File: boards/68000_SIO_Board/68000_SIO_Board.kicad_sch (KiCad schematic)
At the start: 32 parts, among them J1 Conn_01x08, J10 Conn_02x08_Odd_Even, J11 Conn_01x08, J12 Conn_02x04_Odd_Even, J13 Conn_01x10, J14 Conn_02x02_Odd_Even, J2 Conn_01x06, J3 Conn_01x03, J4 Conn_02x10_Odd_Even, J5 Conn_01x06, J6 Conn_01x03, J7 Conn_01x06, J8 Conn_01x06, J9 Conn_01x08, M1 RC2014_40_PIN, U1 74LS138, U2 68681P, U3 68681P, X1 CXO_DIP8

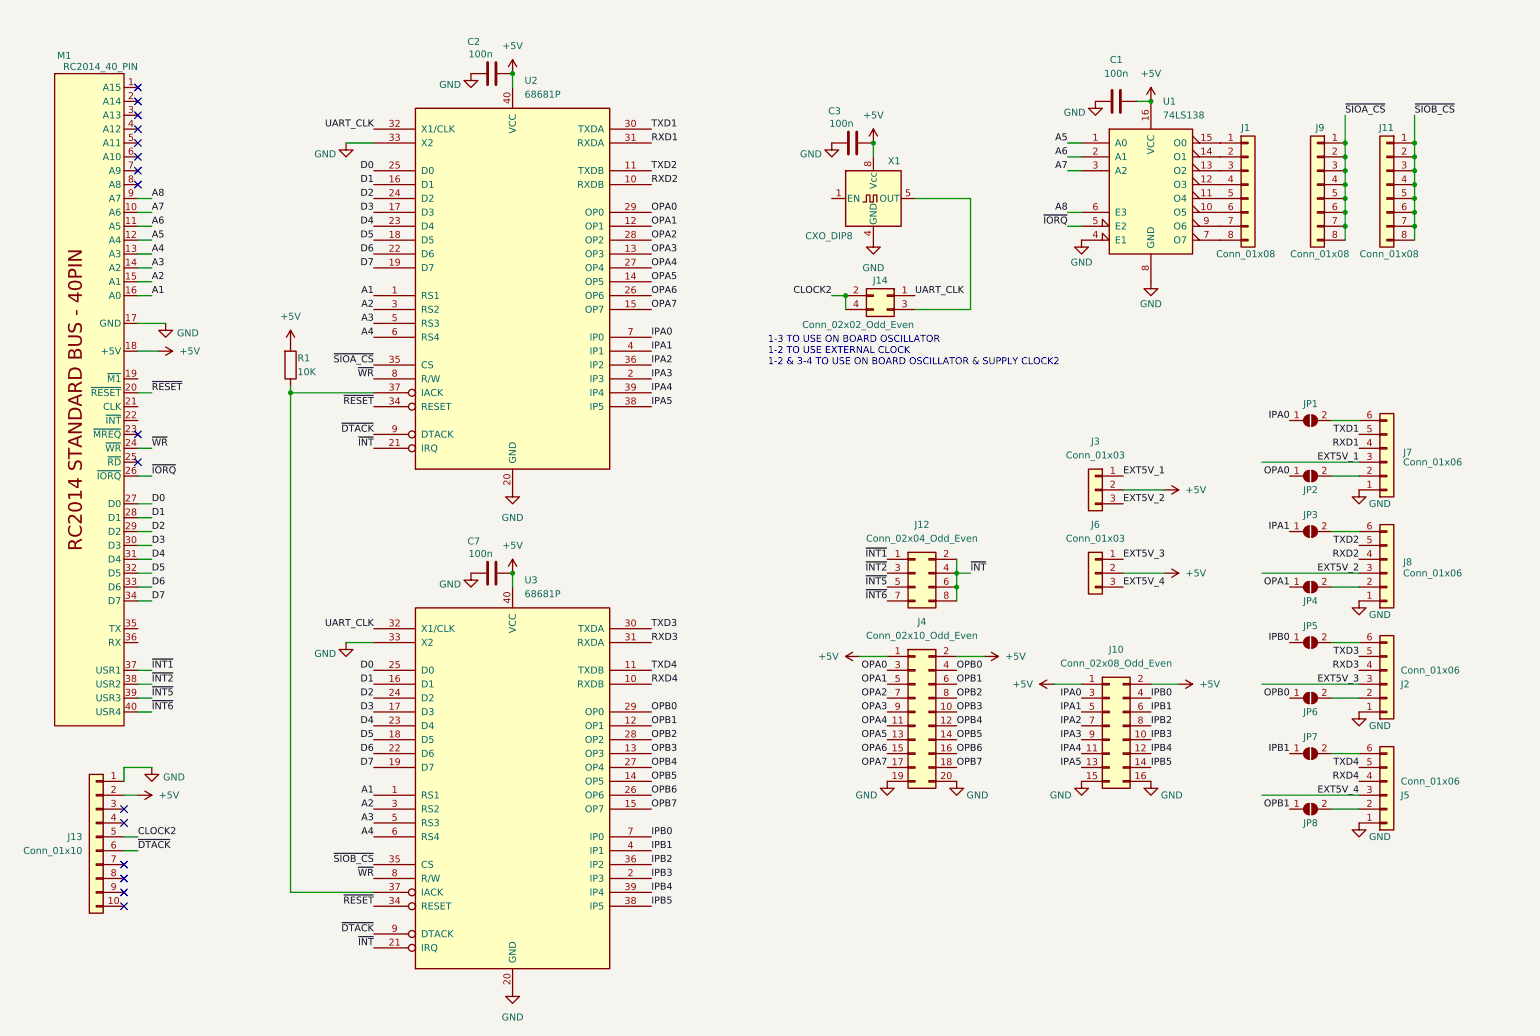
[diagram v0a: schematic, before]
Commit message: Update to v2 board set
Lots of updates to reflect the new v2 boards that use the full RCBus 80 pins as well as slight modifications to the various test programs to reflect the new IO and MEM space addresses.
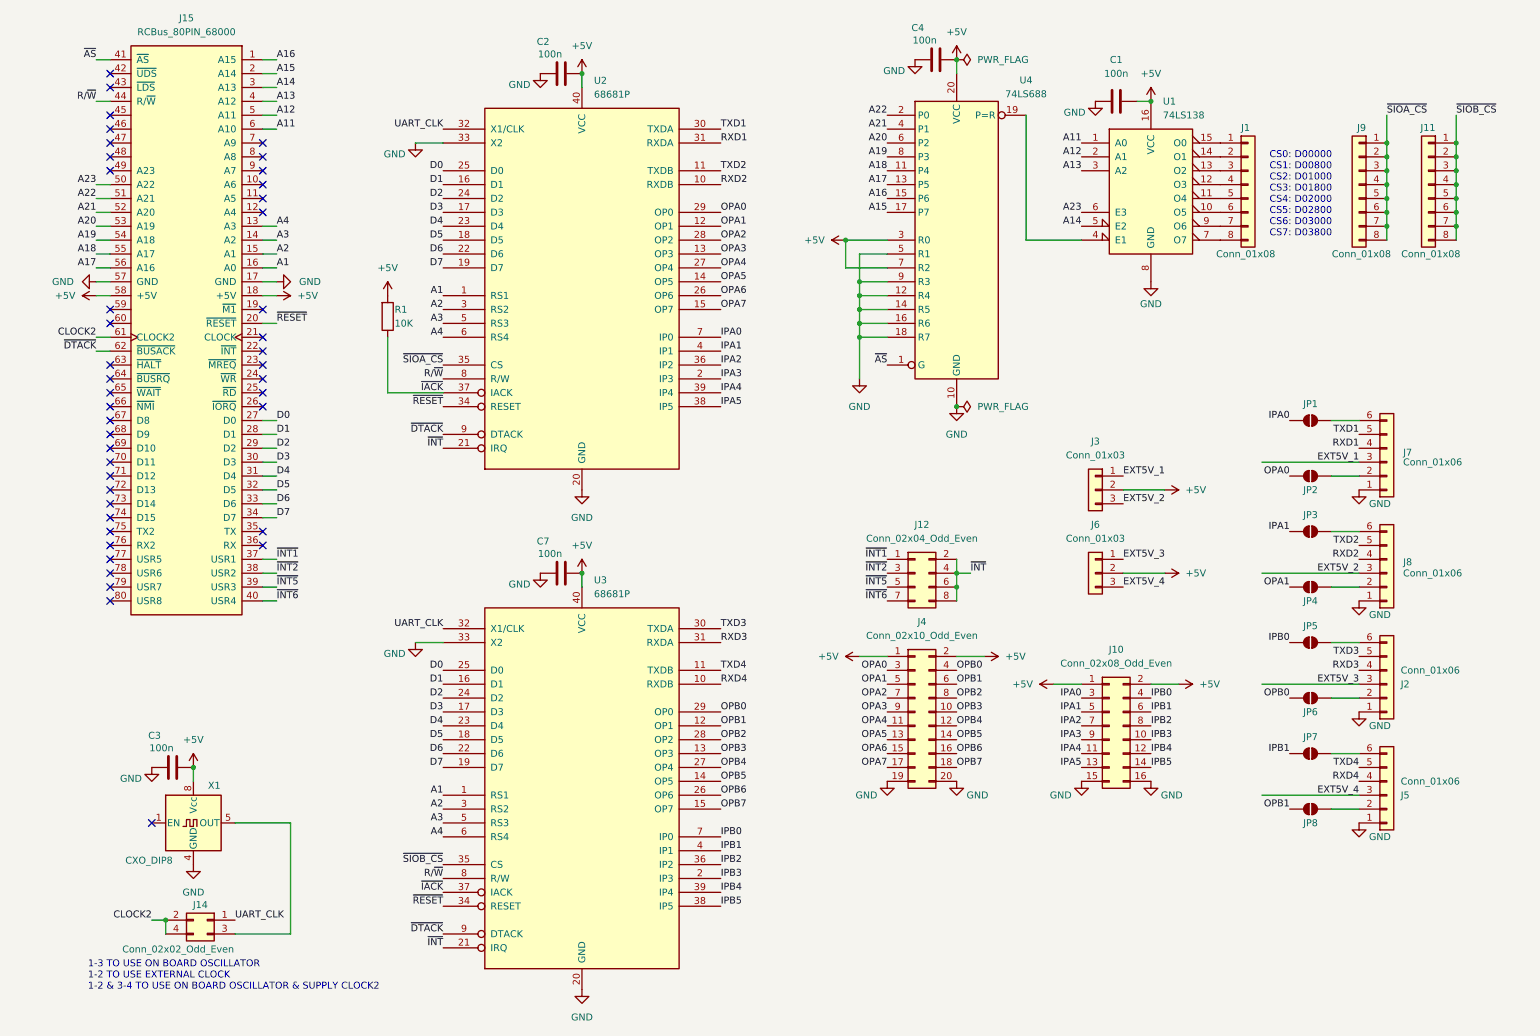
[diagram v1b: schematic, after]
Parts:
- removed J13: Conn_01x10, Connector_PinHeader_2.54mm:PinHeader_1x10_P2.54mm_Vertical, symbol Connector_Generic:Conn_01x10
- removed M1: RC2014_40_PIN, MyLibrary2023:RC2014_STD_40_PIN, symbol MyLibrary2023:RC2014_40_PIN
- added C4: 100n, Capacitor_THT:C_Disc_D5.0mm_W2.5mm_P2.50mm, symbol Device:C
- added J15: RCBus_80PIN_68000, MyLibrary2023:RCBus_80p_Medium, symbol MyLibrary2023:RCBus_80PIN_68000
- added U4: 74LS688, MyLibrary2023:DIP-20_W7.62mm_Socket, symbol 74xx:74LS688
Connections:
- net +5V: now also C4.2, J15.18 (+5V), J15.58 (+5V), U4.20 (VCC), U4.3 (R0), U4.7 (R2)
- net A1: now also J15.16 (A0)
- net A2: now also J15.15 (A1)
- net A3: now also J15.14 (A2)
- net A4: now also J15.13 (A3)
- net CLOCK2: now also J15.61 (CLOCK2)
- net D0: now also J15.27 (D0)
- net D1: now also J15.28 (D1)
- net D2: now also J15.29 (D2)
- net D3: now also J15.30 (D3)
- net D4: now also J15.31 (D4)
- net D5: now also J15.32 (D5)
- net D6: now also J15.33 (D6)
- net D7: now also J15.34 (D7)
- net GND: now also C4.1, J15.17 (GND), J15.57 (GND), U4.10 (GND), U4.12 (R4), U4.14 (R5), U4.16 (R6), U4.18 (R7), U4.5 (R1), U4.9 (R3); no longer U1.4 (E1)
- net ~{DTACK}: now also J15.62 (~{BUSACK})
- net ~{INT1}: now also J15.37 (USR1)
- net ~{INT2}: now also J15.38 (USR2)
- net ~{INT5}: now also J15.39 (USR3)
- net ~{INT6}: now also J15.40 (USR4)
- net ~{RESET}: now also J15.20 (~{RESET})
- net ~{IACK}: now reaches R1.1, U2.37 (IACK), U3.37 (IACK)
- net A5 renamed A11
- net A11: now also J15.6 (A10)
- net A6 renamed A12
- net A12: now also J15.5 (A11)
- net A7 renamed A13
- net A13: now also J15.4 (A12)
- net A8 renamed A23
- net A23: now also J15.50 (A22)
- net ~{IORQ} renamed A14
- net A14: now also J15.3 (A13)
- net ~{WR} renamed R/~{W}
- net R/~{W}: now also J15.44 (R/~{W})
- new net: U1.4 (E1), U4.19 (P=R)
- new net A15: J15.2 (A14), U4.17 (P7)
- new net A16: J15.1 (A15), U4.15 (P6)
- new net A17: J15.56 (A16), U4.13 (P5)
- new net A18: J15.55 (A17), U4.11 (P4)
- new net A19: J15.54 (A18), U4.8 (P3)
- new net A20: J15.53 (A19), U4.6 (P2)
- new net A21: J15.52 (A20), U4.4 (P1)
- new net A22: J15.51 (A21), U4.2 (P0)
- new net ~{AS}: J15.41 (~{AS}), U4.1 (G)
- no-connect marks 16 -> 43
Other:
- note added: "CS0: D00000 CS1: D00800 CS2: D01000 CS3: D01800 CS4: D02000 CS5: D02800 CS6: D03000 CS7: D03800"
- moved on the sheet: C2, C3, C7, J11, J14, J9, R1, U2, U3, X1
